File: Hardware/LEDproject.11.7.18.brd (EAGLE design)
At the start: 160 x 100 mm, 14 parts, among them IC1 ATMEGA328-PU, Y1 16MHz

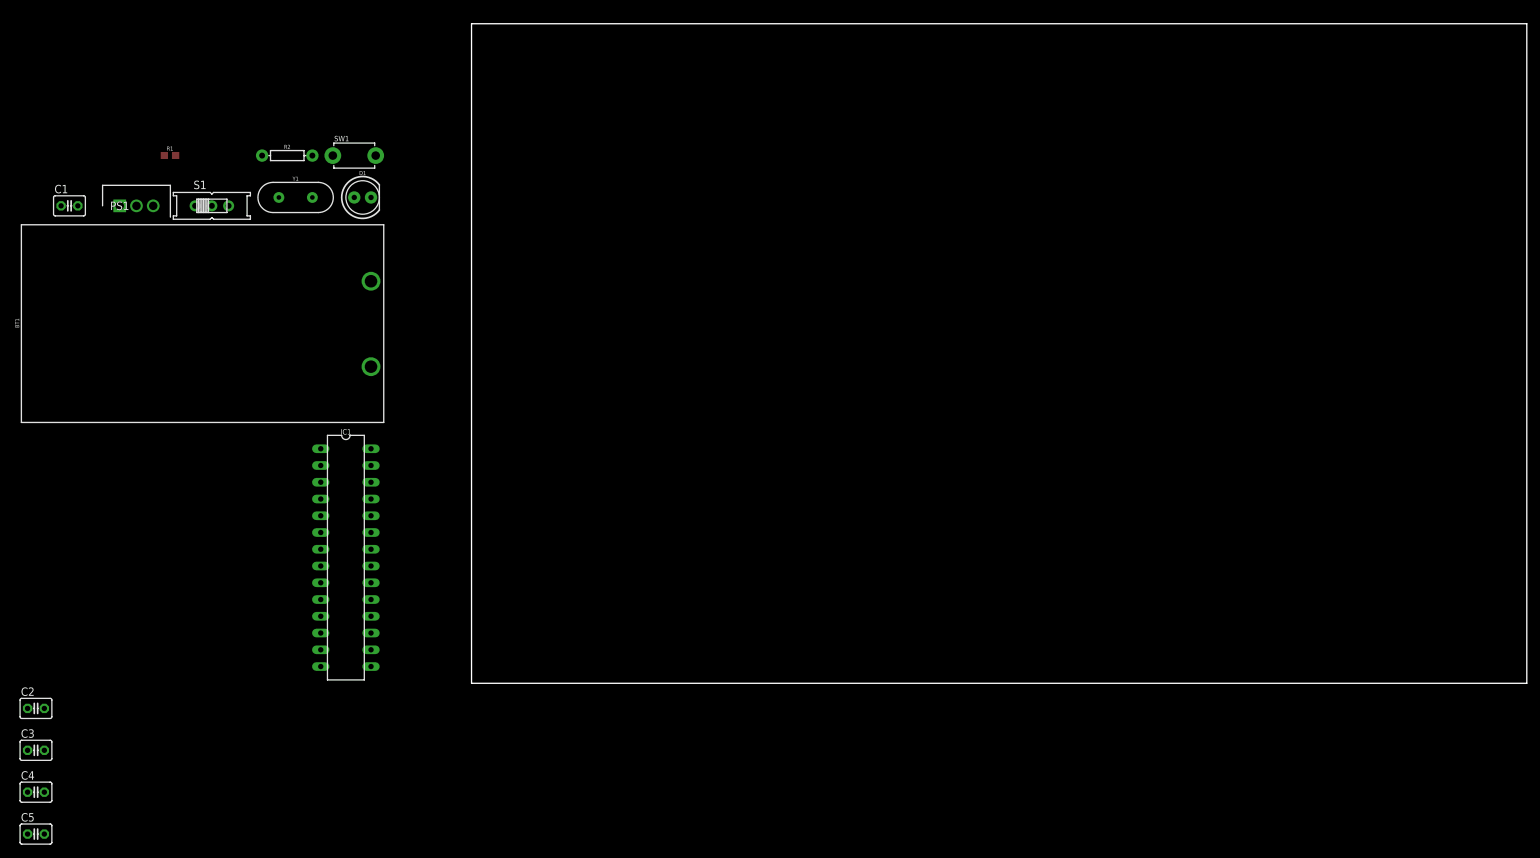
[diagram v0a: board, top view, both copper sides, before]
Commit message: updated breadboard and circuit to match schematics
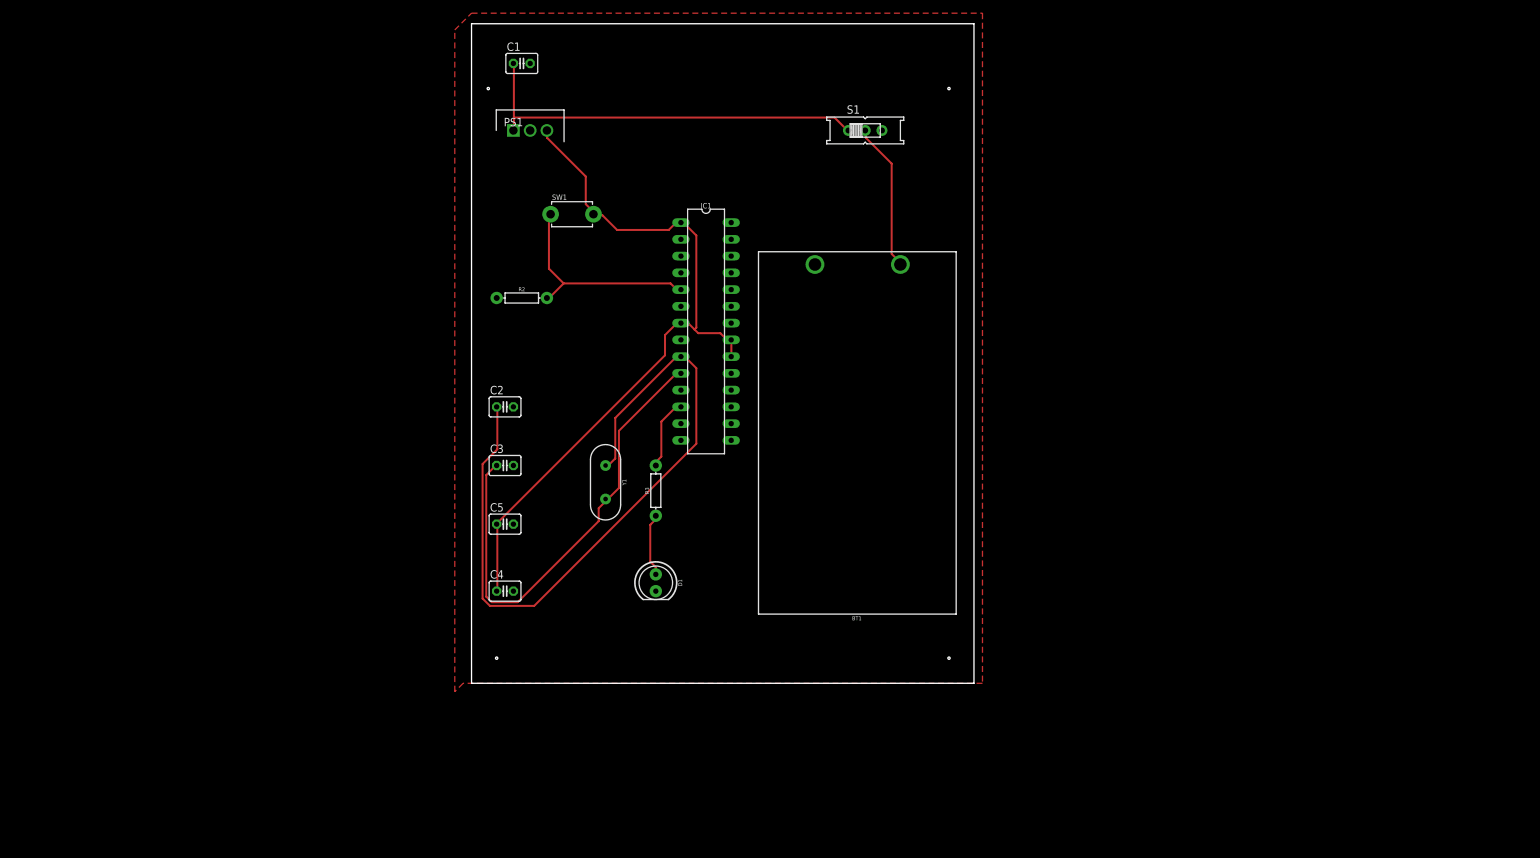
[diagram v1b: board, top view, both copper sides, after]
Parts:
- removed R1: 100 Ohm, SparkFun-Resistors:0603
- added R3: 100 Ohm, SparkFun-Resistors:AXIAL-0.3
- moved S1 99.7 mm to (59.7, 83.8)
- moved C5 85.2 mm to (5.08, 24.1)
- moved C2 84.5 mm to (5.08, 41.9)
- moved C3 83.2 mm to (5.08, 33.0)
- moved C4 77.4 mm to (5.08, 14.0)
- moved D1 73.4 mm to (27.9, 15.2), turned to 270 degrees
- moved C1 71.9 mm to (7.62, 94.0)
- moved BT1 67.4 mm to (52.1, 63.5), turned to 90 degrees
- moved IC1 64.5 mm to (35.6, 53.3)
- moved Y1 63.8 mm to (20.3, 30.5), turned to 270 degrees
- moved PS1 60.8 mm to (6.35, 83.8)
- moved R2 41.6 mm to (7.62, 58.4)
- moved SW1 34.2 mm to (15.2, 71.1)
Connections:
- net N$7: now also R3.P$2; no longer R1.2
- net N$8: now also R3.P$1; no longer R1.1
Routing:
- net +5V: track 0.00 -> 112.0 mm
- net N$1: track 0.00 -> 109.6 mm
- net N$2: track 0.00 -> 71.5 mm
- net N$5: track 0.00 -> 61.8 mm
- net N$6: track 0.00 -> 33.3 mm
- net N$3: track 0.00 -> 22.6 mm
- net N$7: track 0.00 -> 10.9 mm
- net N$8: track 0.00 -> 9.58 mm
- added copper zone on layer 1, net GND
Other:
- board size 160 x 100 mm -> 76.2 x 100 mm
